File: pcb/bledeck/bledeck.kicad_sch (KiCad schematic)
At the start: 37 parts, among them J1 Conn_01x09_Socket, J2 Conn_01x02_Socket, U1 ESP32-DEVKIT-V1

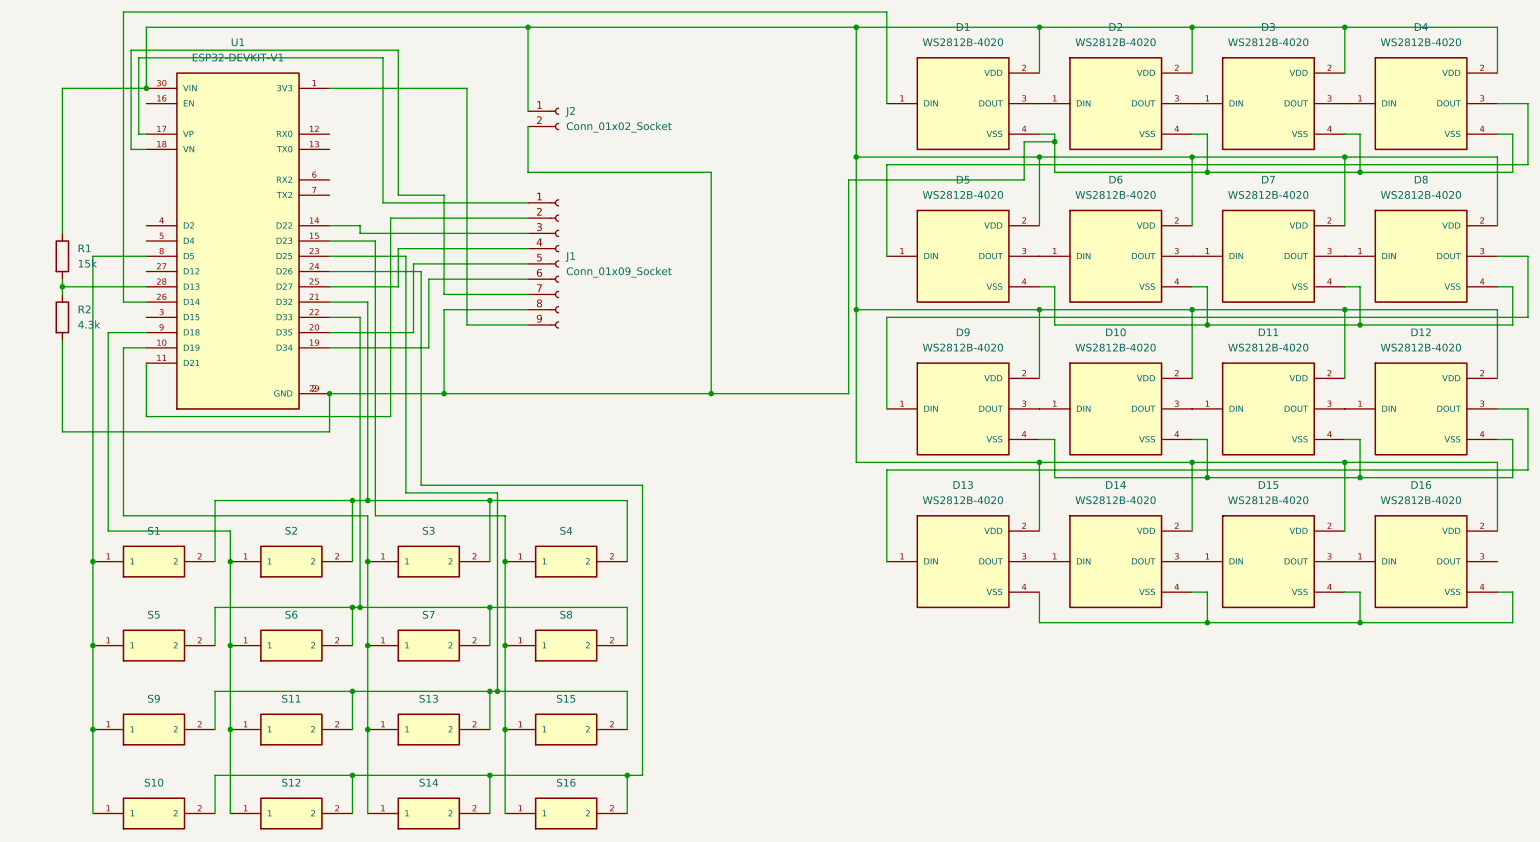
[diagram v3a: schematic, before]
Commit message: [firmware] add battery to display, fix oledupdate [pcb] fix keys connections, fix led traces, fix oled footprint [misc] add parts list to Readme
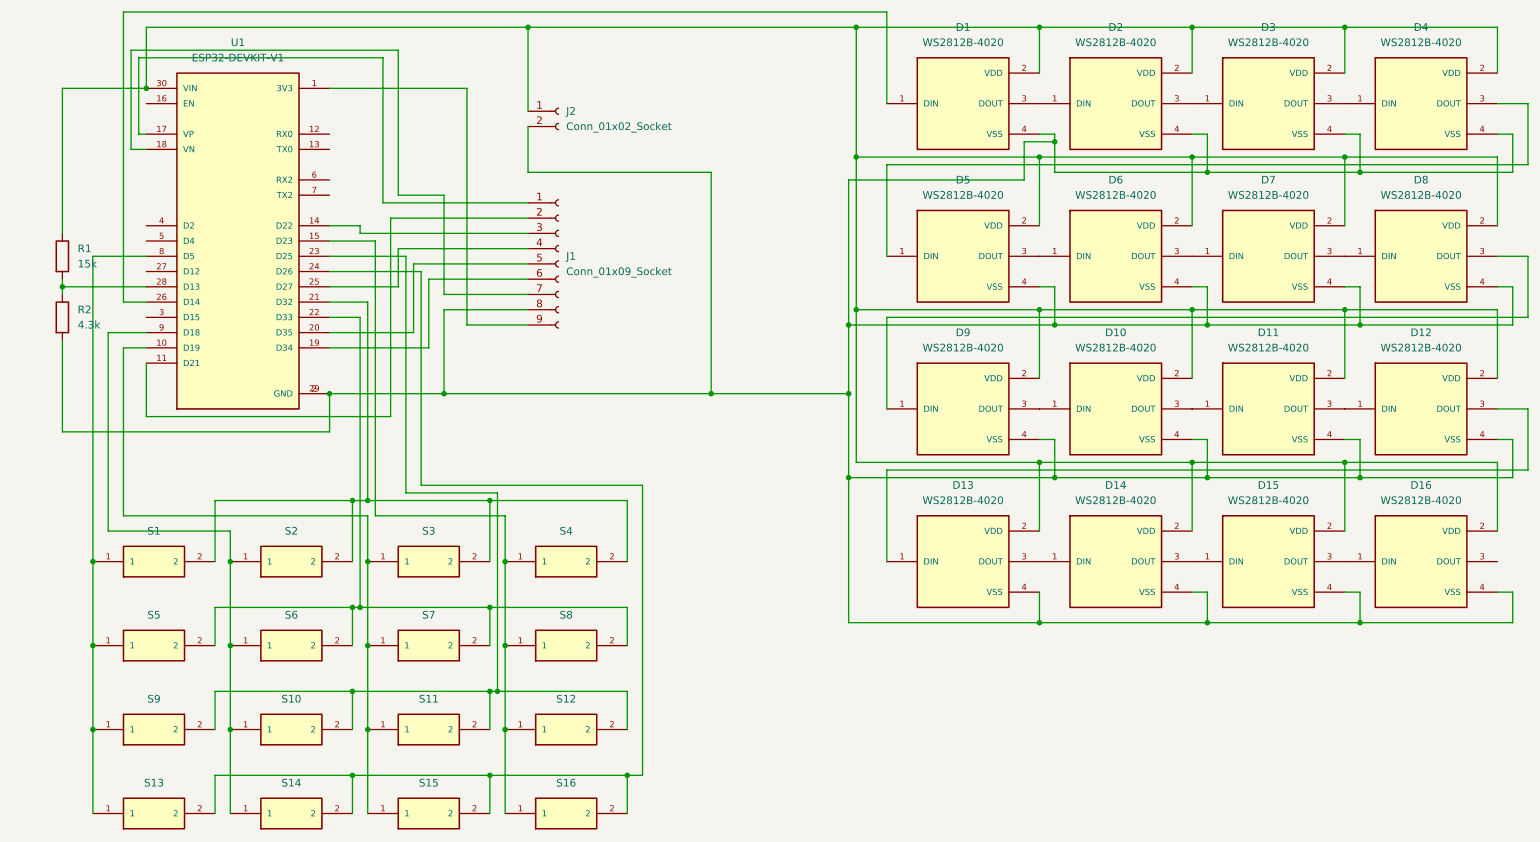
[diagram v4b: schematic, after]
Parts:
- renumbered S11 to S10, S13 to S11, S15 to S12, S10 to S13, S12 to S14, S14 to S15
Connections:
- net at D10.4 (VSS), D11.4 (VSS), D12.4 (VSS)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: now also D1.4 (VSS), D13.4 (VSS), D14.4 (VSS), D15.4 (VSS), D16.4 (VSS), D2.4 (VSS), D3.4 (VSS), D4.4 (VSS), D5.4 (VSS), D6.4 (VSS), D7.4 (VSS), D8.4 (VSS), J1.8 (Pin_8), J2.2 (Pin_2), R2.2, U1.2 (GND), U1.29 (GND)
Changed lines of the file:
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@@
 	(title_block
 		(title "BLEDeck")
-		(date "2025-11-11")
-		(rev "1.0")
+		(date "2025-12-16")
+		(rev "1.1")
 		(company "Davide \"Argaar\" Foschi")
 	)
@@
 	)
 	(junction
+		(at 157.48 110.49)
+		(diameter 0)
+		(color 0 0 0 0)
+	)
+	(junction
 		(at 40.64 45.72)
 		(diameter 0)
@@
 	)
 	(junction
+		(at 157.48 85.09)
+		(diameter 0)
+		(color 0 0 0 0)
+	)
+	(junction
 		(at 242.57 59.69)
 		(diameter 0)
@@
 	)
 	(junction
+		(at 191.77 110.49)
+		(diameter 0)
+		(color 0 0 0 0)
+	)
+	(junction
 		(at 240.03 107.95)
 		(diameter 0)
@@
 	)
 	(junction
+		(at 157.48 96.52)
+		(diameter 0)
+		(color 0 0 0 0)
+	)
+	(junction
 		(at 76.2 132.08)
 		(diameter 0)
@@
 	)
 	(junction
+		(at 189.23 134.62)
+		(diameter 0)
+		(color 0 0 0 0)
+	)
+	(junction
 		(at 214.63 82.55)
 		(diameter 0)
@@
 	)
 	(junction
+		(at 191.77 85.09)
+		(diameter 0)
+		(color 0 0 0 0)
+	)
+	(junction
 		(at 214.63 107.95)
 		(diameter 0)
@@
 	(wire
 		(pts
+			(xy 157.48 110.49) (xy 157.48 134.62)
+		)
+		(stroke
+			(width 0)
+			(type default)
+		)
+	)
+	(wire
+		(pts
 			(xy 123.19 160.02) (xy 120.65 160.02)
 		)
@@
 	(wire
 		(pts
+			(xy 157.48 96.52) (xy 157.48 110.49)
+		)
+		(stroke
+			(width 0)
+			(type default)
+		)
+	)
+	(wire
+		(pts
 			(xy 39.37 40.64) (xy 39.37 53.34)
 		)
@@
 	(wire
 		(pts
-			(xy 157.48 96.52) (xy 157.48 60.96)
+			(xy 157.48 96.52) (xy 157.48 85.09)
 		)
 		(stroke
@@
 	(wire
 		(pts
+			(xy 157.48 85.09) (xy 191.77 85.09)
+		)
+		(stroke
+			(width 0)
+			(type default)
+		)
+	)
+	(wire
+		(pts
 			(xy 214.63 57.15) (xy 240.03 57.15)
 		)
@@
 	(wire
 		(pts
+			(xy 191.77 110.49) (xy 157.48 110.49)
+		)
+		(stroke
+			(width 0)
+			(type default)
+		)
+	)
+	(wire
+		(pts
 			(xy 270.51 109.22) (xy 270.51 99.06)
 		)
@@
 	(wire
 		(pts
+			(xy 157.48 85.09) (xy 157.48 60.96)
+		)
+		(stroke
+			(width 0)
+			(type default)
+		)
+	)
+	(wire
+		(pts
 			(xy 265.43 53.34) (xy 267.97 53.34)
 		)
@@
 	(wire
 		(pts
+			(xy 189.23 134.62) (xy 157.48 134.62)
+		)
+		(stroke
+			(width 0)
+			(type default)
+		)
+	)
+	(wire
+		(pts
 			(xy 214.63 35.56) (xy 240.03 35.56)
 		)
@@
 		(dnp no)
 		(fields_autoplaced yes)
-		(property "Reference" "S11"
+		(property "Reference" "S10"
 			(at 64.77 147.32 0)
 			(effects
@@
 			(project "bledeck"
 				(path "/8bba6075-8a84-4835-a7b9-00f9c9f191ba"
-					(reference "S11")
+					(reference "S10")
 					(unit 1)
 				)
@@
 		(dnp no)
 		(fields_autoplaced yes)
-		(property "Reference" "S13"
+		(property "Reference" "S11"
 			(at 87.63 147.32 0)
 			(effects
@@
 			(project "bledeck"
 				(path "/8bba6075-8a84-4835-a7b9-00f9c9f191ba"
-					(reference "S13")
+					(reference "S11")
 					(unit 1)
 				)
@@
 		(dnp no)
 		(fields_autoplaced yes)
-		(property "Reference" "S15"
+		(property "Reference" "S12"
 			(at 110.49 147.32 0)
 			(effects
@@
 			(project "bledeck"
 				(path "/8bba6075-8a84-4835-a7b9-00f9c9f191ba"
-					(reference "S15")
+					(reference "S12")
 					(unit 1)
 				)
@@
 		(dnp no)
 		(fields_autoplaced yes)
-		(property "Reference" "S10"
+		(property "Reference" "S13"
 			(at 41.91 161.29 0)
 			(effects
@@
 			(project "bledeck"
 				(path "/8bba6075-8a84-4835-a7b9-00f9c9f191ba"
-					(reference "S10")
+					(reference "S13")
 					(unit 1)
 				)
@@
 		(dnp no)
 		(fields_autoplaced yes)
-		(property "Reference" "S14"
+		(property "Reference" "S15"
 			(at 87.63 161.29 0)
 			(effects
@@
 			(project "bledeck"
 				(path "/8bba6075-8a84-4835-a7b9-00f9c9f191ba"
-					(reference "S14")
+					(reference "S15")
 					(unit 1)
 				)
@@
 		(dnp no)
 		(fields_autoplaced yes)
-		(property "Reference" "S12"
+		(property "Reference" "S14"
 			(at 64.77 161.29 0)
 			(effects
@@
 			(project "bledeck"
 				(path "/8bba6075-8a84-4835-a7b9-00f9c9f191ba"
-					(reference "S12")
+					(reference "S14")
 					(unit 1)
 				)

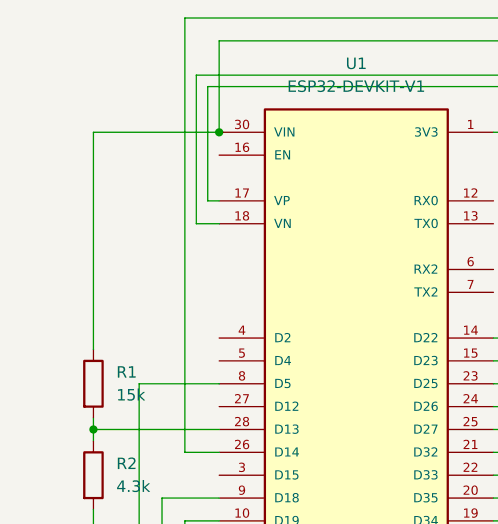
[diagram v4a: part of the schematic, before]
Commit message: [pcb] version 1.1 [firmware] enabled 16 rgb, change keys layout
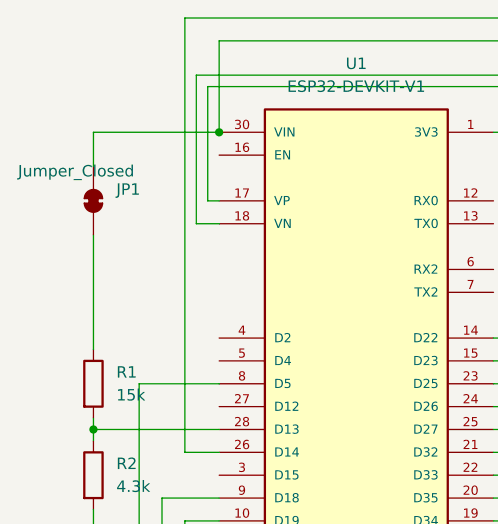
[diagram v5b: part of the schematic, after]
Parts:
- added JP1: Jumper_Closed, BLEDeck:PinHeader_1x02_P2.54mm_Vertical, symbol Jumper:SolderJumper_2_Bridged
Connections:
- net at D1.2 (VDD), D10.2 (VDD), D11.2 (VDD)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: now also JP1.2 (B); no longer R1.1
- new net: JP1.1 (A), R1.1
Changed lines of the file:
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@@
-	(wire
-		(pts
-			(xy 26.67 45.72) (xy 26.67 69.85)
-		)
-		(stroke
-			(width 0)
-			(type default)
-		)
-	)
 	(wire
 		(pts
@@
 	(wire
 		(pts
+			(xy 26.67 57.15) (xy 26.67 69.85)
+		)
+		(stroke
+			(width 0)
+			(type default)
+		)
+	)
+	(wire
+		(pts
 			(xy 86.36 111.76) (xy 123.19 111.76)
 		)
@@
 		(pts
 			(xy 189.23 35.56) (xy 189.23 43.18)
+		)
+		(stroke
+			(width 0)
+			(type default)
+		)
+	)
+	(wire
+		(pts
+			(xy 26.67 45.72) (xy 26.67 49.53)
 		)
 		(stroke
@@
 					(unit 1)
 				)
+			)
+		)
+	)
+	(symbol
+		(lib_id "Jumper:SolderJumper_2_Bridged")
+		(at 26.67 53.34 90)
+		(unit 1)
+		(exclude_from_sim no)
+		(in_bom no)
+		(on_board yes)
+		(dnp no)
+		(property "Reference" "JP1"
+			(at 29.21 52.0699 90)
+			(effects
+				(font
+					(size 1.27 1.27)
+				)
+				(justify right)
+			)
+		)
+		(property "Value" "Jumper_Closed"
+			(at 18.288 50.038 90)
+			(effects
+				(font
+					(size 1.27 1.27)
+				)
+				(justify right)
+			)
+		)
+		(property "Footprint" "BLEDeck:PinHeader_1x02_P2.54mm_Vertical"
+			(at 26.67 53.34 0)
+			(effects
+				(font
+					(size 1.27 1.27)
+				)
+				(hide yes)
+			)
+		)
+		(property "Datasheet" "~"
+			(at 26.67 53.34 0)
+			(effects
+				(font
+					(size 1.27 1.27)
+				)
+				(hide yes)
+			)
+		)
+		(property "Description" "Solder Jumper, 2-pole, closed/bridged"
+			(at 26.67 53.34 0)
+			(effects
+				(font
+					(size 1.27 1.27)
+				)
+				(hide yes)
+			)
+		)
+		(pin "2"
+		)
+		(pin "1"
+		)
+		(instances
+			(project ""
+				(path "/8bba6075-8a84-4835-a7b9-00f9c9f191ba"
+					(reference "JP1")
+					(unit 1)
+				)
